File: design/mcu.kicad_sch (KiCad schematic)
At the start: 13 parts, among them U1 STM32F40X_LQFP64, X1 8m

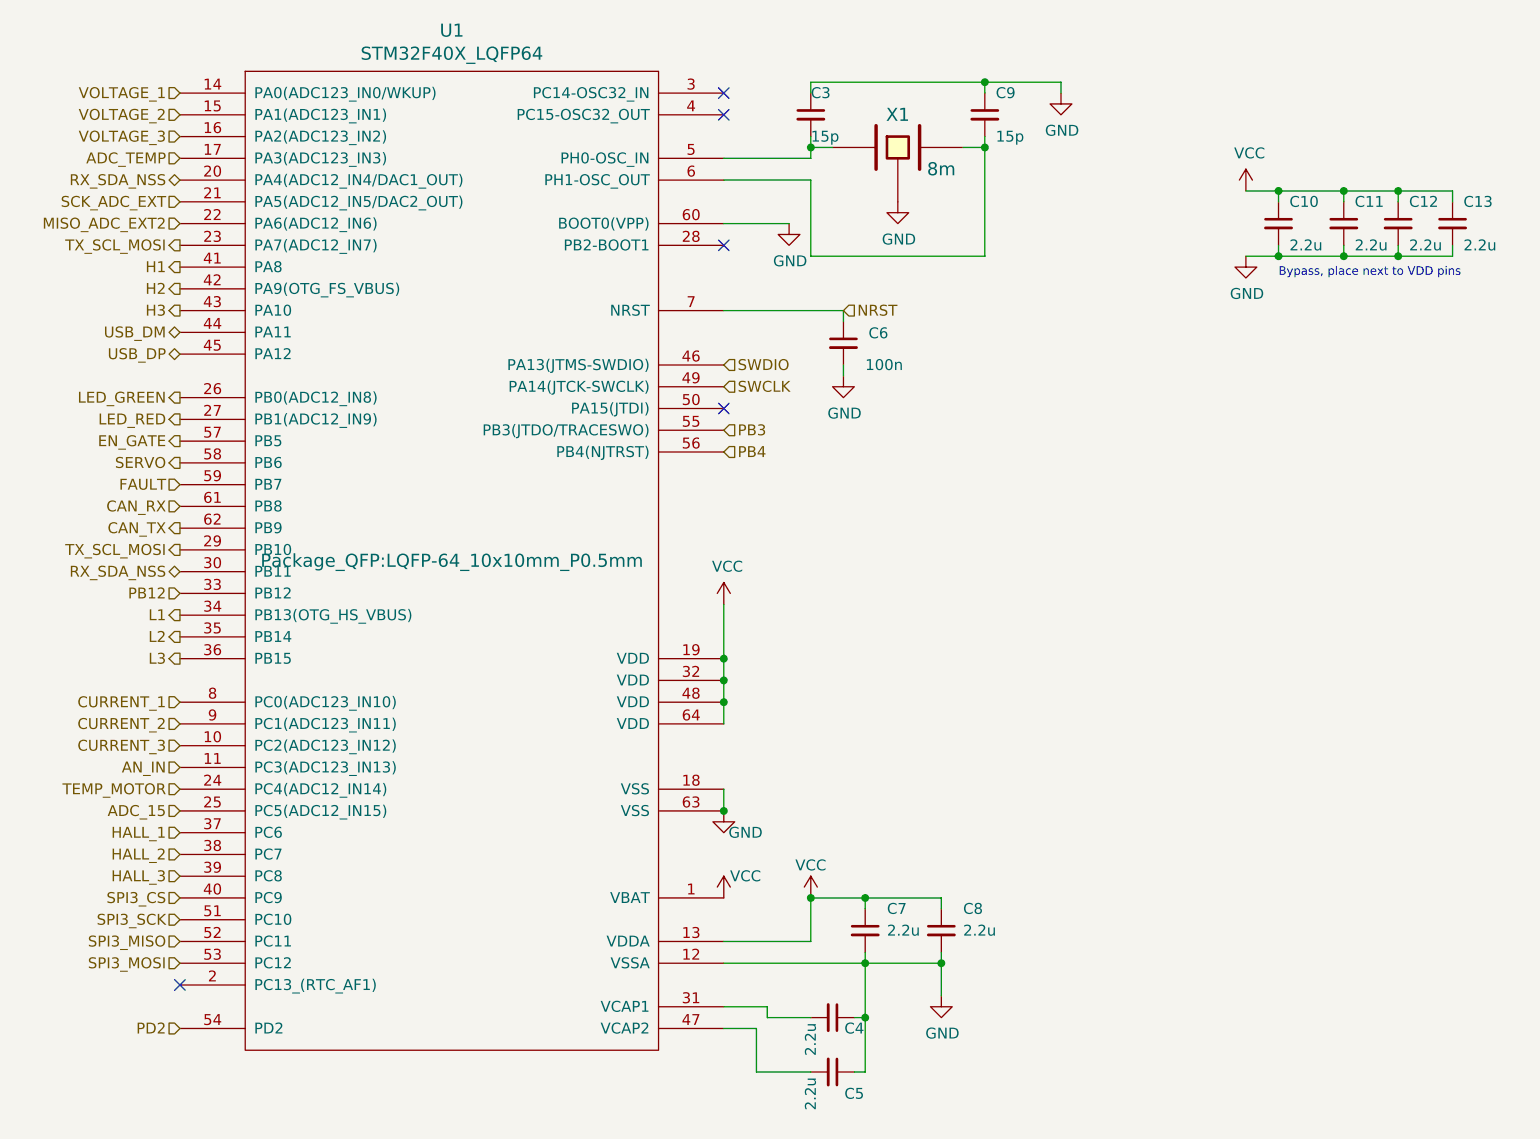
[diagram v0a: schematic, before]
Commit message: Impresión de esquemático en pdf
Impresión de la versión del esquemático en la carpeta /pdf
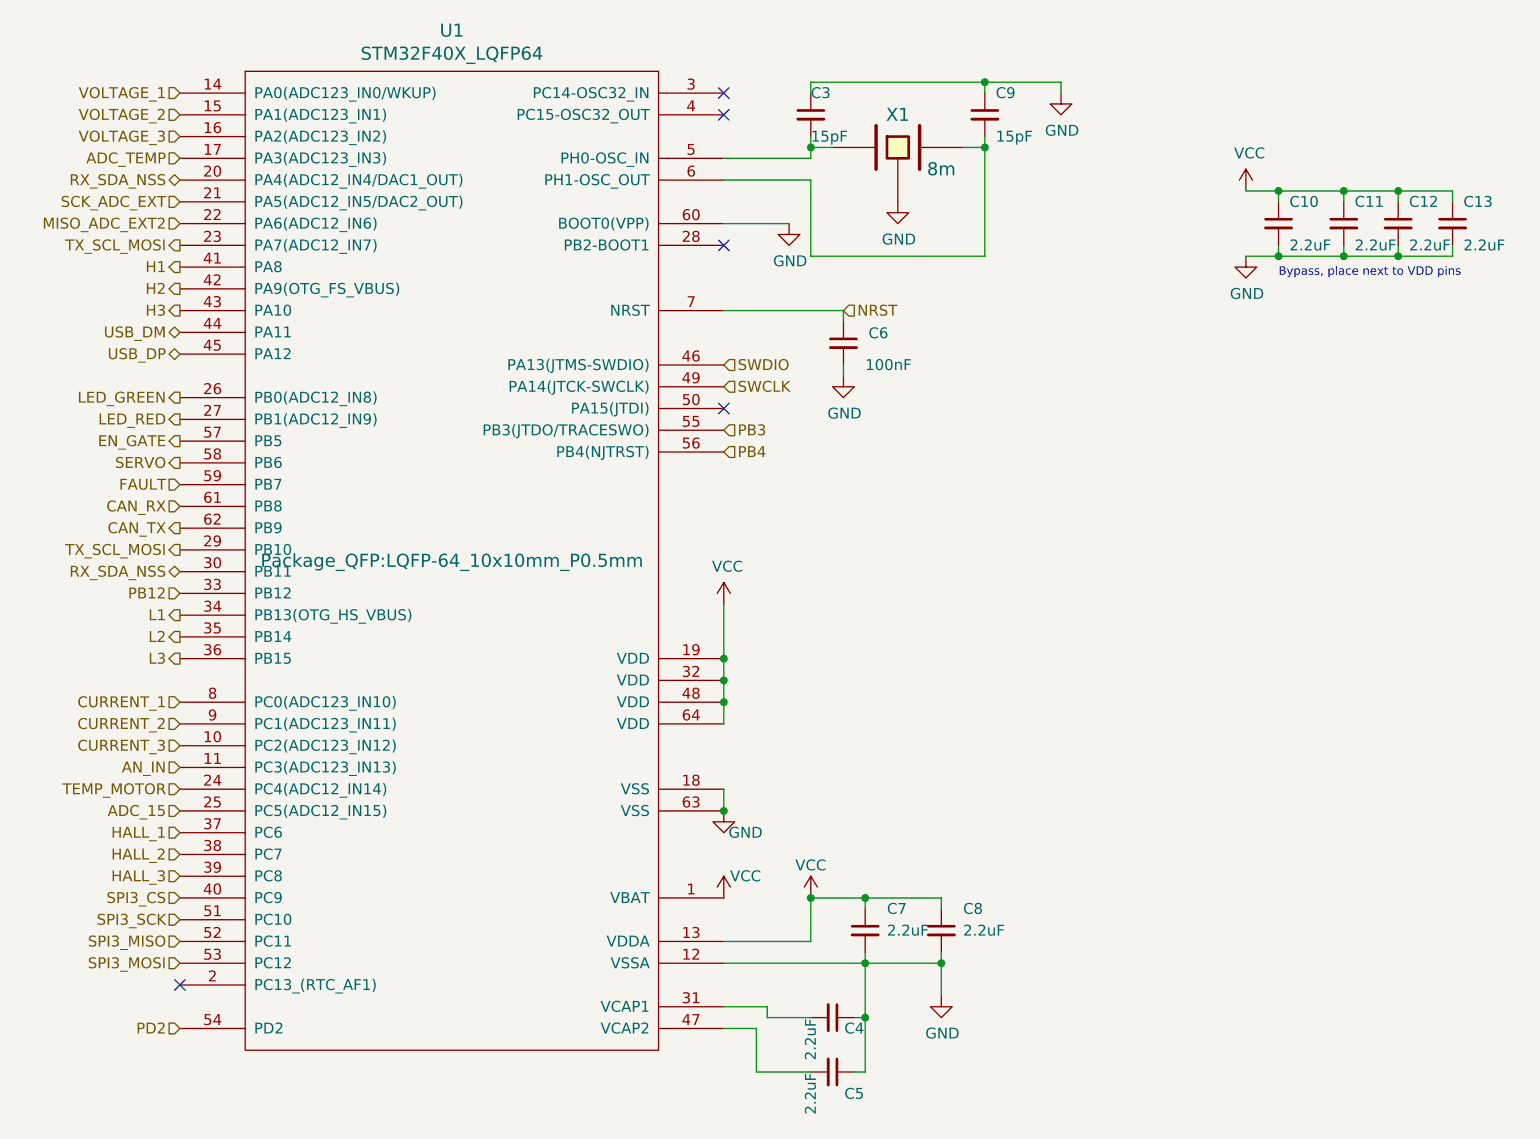
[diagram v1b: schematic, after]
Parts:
- C10, C11, C12, C13, C4, C5, C7, C8: value 2.2u -> 2.2uF
- C3, C9: value 15p -> 15pF
- C6: value 100n -> 100nF
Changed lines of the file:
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@@
 			)
 		)
-		(property "Value" "15p"
+		(property "Value" "15pF"
 			(at 195.58 36.83 0)
 			(effects
@@
 			)
 		)
-		(property "Value" "15p"
+		(property "Value" "15pF"
 			(at 217.17 36.83 0)
 			(effects
@@
 			)
 		)
-		(property "Value" "100n"
+		(property "Value" "100nF"
 			(at 201.93 63.5 0)
 			(effects
@@
 			)
 		)
-		(property "Value" "2.2u"
+		(property "Value" "2.2uF"
 			(at 204.47 129.54 0)
 			(effects
@@
 			)
 		)
-		(property "Value" "2.2u"
+		(property "Value" "2.2uF"
 			(at 213.36 129.54 0)
 			(effects
@@
 			)
 		)
-		(property "Value" "2.2u"
+		(property "Value" "2.2uF"
 			(at 195.58 142.24 0)
 			(effects
@@
 			)
 		)
-		(property "Value" "2.2u"
+		(property "Value" "2.2uF"
 			(at 195.58 148.59 0)
 			(effects
@@
 			)
 		)
-		(property "Value" "2.2u"
+		(property "Value" "2.2uF"
 			(at 251.46 49.53 0)
 			(effects
@@
 			)
 		)
-		(property "Value" "2.2u"
+		(property "Value" "2.2uF"
 			(at 259.08 49.53 0)
 			(effects
@@
 			)
 		)
-		(property "Value" "2.2u"
+		(property "Value" "2.2uF"
 			(at 265.43 49.53 0)
 			(effects
@@
 			)
 		)
-		(property "Value" "2.2u"
+		(property "Value" "2.2uF"
 			(at 271.78 49.53 0)
 			(effects

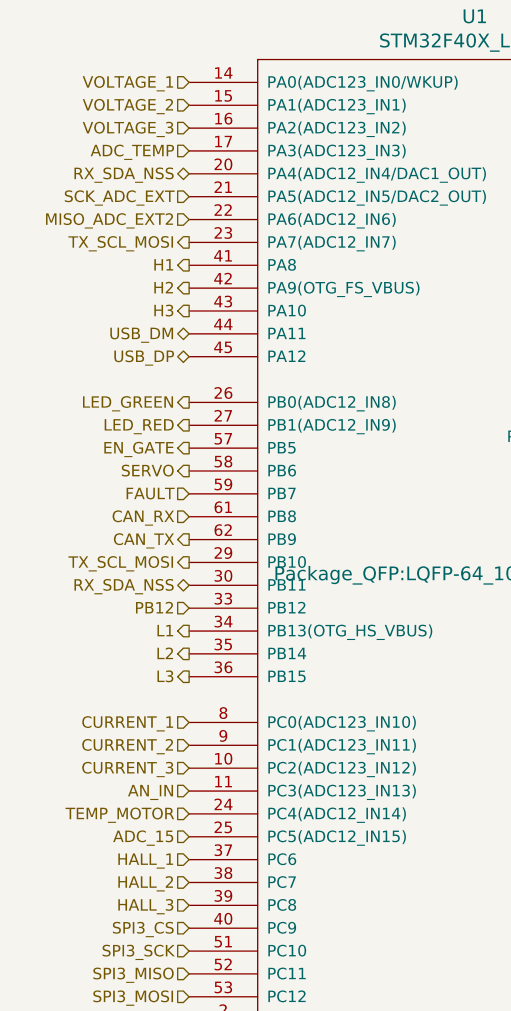
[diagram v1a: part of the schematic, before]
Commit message: Pequeños cambios
Se sacaron y se marcaron como NC:
	* CAN_TX y CAN_RX (no se usa CAN).
	* SERVO (no vamos a manejar servomotores).
	* ADC_15, MISO_ADC_EXT, TX_SCL_MOSI, RX_SDA_NSS, SCK_ADC_EXT (sin ADC externo ni acelerómetro).
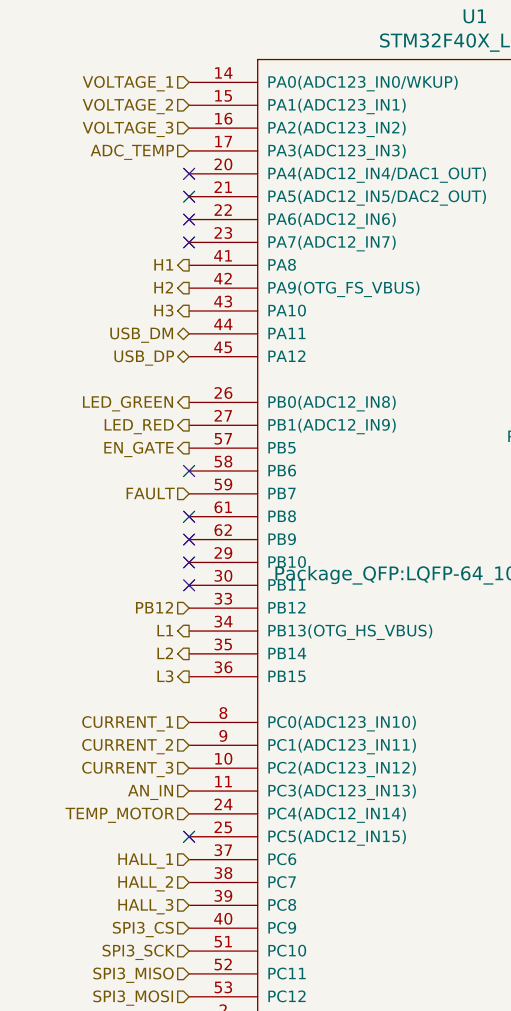
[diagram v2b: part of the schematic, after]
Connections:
- net ADC_15: no longer names the net of U1.25 (PC5(ADC12_IN15))
- net CAN_RX: no longer names the net of U1.61 (PB8)
- net CAN_TX: no longer names the net of U1.62 (PB9)
- net MISO_ADC_EXT2: no longer names the net of U1.22 (PA6(ADC12_IN6))
- net RX_SDA_NSS: no longer names the net of U1.20 (PA4(ADC12_IN4/DAC1_OUT))
- net RX_SDA_NSS: no longer U1.30 (PB11)
- net SCK_ADC_EXT: no longer names the net of U1.21 (PA5(ADC12_IN5/DAC2_OUT))
- net SERVO: no longer names the net of U1.58 (PB6)
- net TX_SCL_MOSI: no longer names the net of U1.23 (PA7(ADC12_IN7))
- net TX_SCL_MOSI: no longer U1.29 (PB10)
- no-connect marks 5 -> 15
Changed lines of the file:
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@@
+	)
+	(no_connect
+		(at 121.92 80.01)
+	)
+	(no_connect
+		(at 121.92 82.55)
+	)
+	(no_connect
+		(at 121.92 115.57)
+	)
+	(no_connect
+		(at 121.92 41.91)
 	)
 	(no_connect
@@
 	)
 	(no_connect
+		(at 121.92 85.09)
+	)
+	(no_connect
+		(at 121.92 44.45)
+	)
+	(no_connect
+		(at 121.92 49.53)
+	)
+	(no_connect
 		(at 185.42 68.58)
+	)
+	(no_connect
+		(at 121.92 87.63)
 	)
 	(no_connect
@@
 	)
 	(no_connect
+		(at 121.92 46.99)
+	)
+	(no_connect
 		(at 185.42 34.29)
+	)
+	(no_connect
+		(at 121.92 74.93)
 	)
 	(wire
@@
 		)
 	)
-	(hierarchical_label "RX_SDA_NSS"
-		(shape bidirectional)
-		(at 121.92 41.91 180)
-		(fields_autoplaced yes)
-		(effects
-			(font
-				(size 1.27 1.27)
-			)
-			(justify right)
-		)
-	)
 	(hierarchical_label "ADC_TEMP"
 		(shape input)
@@
 		)
 	)
-	(hierarchical_label "MISO_ADC_EXT2"
-		(shape input)
-		(at 121.92 46.99 180)
-		(fields_autoplaced yes)
-		(effects
-			(font
-				(size 1.27 1.27)
-			)
-			(justify right)
-		)
-	)
 	(hierarchical_label "AN_IN"
 		(shape input)
@@
 		)
 	)
-	(hierarchical_label "SERVO"
-		(shape output)
-		(at 121.92 74.93 180)
-		(fields_autoplaced yes)
-		(effects
-			(font
-				(size 1.27 1.27)
-			)
-			(justify right)
-		)
-	)
-	(hierarchical_label "SCK_ADC_EXT"
-		(shape input)
-		(at 121.92 44.45 180)
-		(fields_autoplaced yes)
-		(effects
-			(font
-				(size 1.27 1.27)
-			)
-			(justify right)
-		)
-	)
 	(hierarchical_label "PB4"
 		(shape input)
@@
 		)
 	)
-	(hierarchical_label "TX_SCL_MOSI"
-		(shape output)
-		(at 121.92 85.09 180)
-		(fields_autoplaced yes)
-		(effects
-			(font
-				(size 1.27 1.27)
-			)
-			(justify right)
-		)
-	)
 	(hierarchical_label "SWDIO"
 		(shape input)
@@
 		)
 	)
-	(hierarchical_label "TX_SCL_MOSI"
-		(shape output)
-		(at 121.92 49.53 180)
-		(fields_autoplaced yes)
-		(effects
-			(font
-				(size 1.27 1.27)
-			)
-			(justify right)
-		)
-	)
 	(hierarchical_label "SWCLK"
 		(shape input)
@@
 		)
 	)
-	(hierarchical_label "RX_SDA_NSS"
-		(shape bidirectional)
-		(at 121.92 87.63 180)
-		(fields_autoplaced yes)
-		(effects
-			(font
-				(size 1.27 1.27)
-			)
-			(justify right)
-		)
-	)
 	(hierarchical_label "TEMP_MOTOR"
 		(shape input)
@@
 		)
 	)
-	(hierarchical_label "CAN_TX"
-		(shape output)
-		(at 121.92 82.55 180)
-		(fields_autoplaced yes)
-		(effects
-			(font
-				(size 1.27 1.27)
-			)
-			(justify right)
-		)
-	)
 	(hierarchical_label "EN_GATE"
 		(shape output)
@@
 		)
 	)
-	(hierarchical_label "ADC_15"
-		(shape input)
-		(at 121.92 115.57 180)
-		(fields_autoplaced yes)
-		(effects
-			(font
-				(size 1.27 1.27)
-			)
-			(justify right)
-		)
-	)
 	(hierarchical_label "HALL_1"
 		(shape input)
@@
 		(fields_autoplaced yes)
 		(effects
-			(font
-				(size 1.27 1.27)
-			)
-			(justify right)
-		)
-	)
-	(hierarchical_label "CAN_RX"
-		(shape input)
-		(at 121.92 80.01 180)
-		(fields_autoplaced yes)
-		(effects

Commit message: Agrego MFR.Part # a capacitores
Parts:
- C10, C11, C12, C13, C4, C5, C7, C8: Manufacturer (none) -> Samsung Electro-Mechanics; Manufacturer Product Number  (none) -> CL10A225KO8NNNC
- C3, C9: Manufacturer (none) -> Samsung Electro-Mechanics; Manufacturer Product Number  (none) -> CL10C150JB8NNNC
- C6: Manufacturer (none) -> YAGEO; Manufacturer Product Number  (none) -> CC0603KRX7R9BB104
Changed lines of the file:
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@@
+			)
+		)
+		(property "Manufacturer" "Samsung Electro-Mechanics"
+			(at 195.58 34.29 0)
+			(effects
+				(font
+					(size 1.27 1.27)
+				)
+				(hide yes)
+			)
+		)
+		(property "Manufacturer Product Number " "CL10C150JB8NNNC"
+			(at 195.58 34.29 0)
+			(effects
+				(font
+					(size 1.27 1.27)
+				)
+				(hide yes)
 			)
 		)
@@
 			)
 		)
+		(property "Manufacturer" "Samsung Electro-Mechanics"
+			(at 215.9 34.29 0)
+			(effects
+				(font
+					(size 1.27 1.27)
+				)
+				(hide yes)
+			)
+		)
+		(property "Manufacturer Product Number " "CL10C150JB8NNNC"
+			(at 215.9 34.29 0)
+			(effects
+				(font
+					(size 1.27 1.27)
+				)
+				(hide yes)
+			)
+		)
 		(pin "1"
 		)
@@
 			)
 		)
+		(property "Manufacturer" "YAGEO"
+			(at 199.39 60.96 0)
+			(effects
+				(font
+					(size 1.27 1.27)
+				)
+				(hide yes)
+			)
+		)
+		(property "Manufacturer Product Number " "CC0603KRX7R9BB104"
+			(at 199.39 60.96 0)
+			(effects
+				(font
+					(size 1.27 1.27)
+				)
+				(hide yes)
+			)
+		)
 		(pin "2"
 		)
@@
 			)
 		)
+		(property "Manufacturer" "Samsung Electro-Mechanics"
+			(at 201.93 129.54 0)
+			(effects
+				(font
+					(size 1.27 1.27)
+				)
+				(hide yes)
+			)
+		)
+		(property "Manufacturer Product Number " "CL10A225KO8NNNC"
+			(at 201.93 129.54 0)
+			(effects
+				(font
+					(size 1.27 1.27)
+				)
+				(hide yes)
+			)
+		)
 		(pin "1"
 		)
@@
 			)
 		)
+		(property "Manufacturer" "Samsung Electro-Mechanics"
+			(at 210.82 129.54 0)
+			(effects
+				(font
+					(size 1.27 1.27)
+				)
+				(hide yes)
+			)
+		)
+		(property "Manufacturer Product Number " "CL10A225KO8NNNC"
+			(at 210.82 129.54 0)
+			(effects
+				(font
+					(size 1.27 1.27)
+				)
+				(hide yes)
+			)
+		)
 		(pin "1"
 		)
@@
 			)
 		)
+		(property "Manufacturer" "Samsung Electro-Mechanics"
+			(at 198.12 139.7 0)
+			(effects
+				(font
+					(size 1.27 1.27)
+				)
+				(hide yes)
+			)
+		)
+		(property "Manufacturer Product Number " "CL10A225KO8NNNC"
+			(at 198.12 139.7 0)
+			(effects
+				(font
+					(size 1.27 1.27)
+				)
+				(hide yes)
+			)
+		)
 		(pin "2"
 		)
@@
 			)
 		)
+		(property "Manufacturer" "Samsung Electro-Mechanics"
+			(at 198.12 146.05 0)
+			(effects
+				(font
+					(size 1.27 1.27)
+				)
+				(hide yes)
+			)
+		)
+		(property "Manufacturer Product Number " "CL10A225KO8NNNC"
+			(at 198.12 146.05 0)
+			(effects
+				(font
+					(size 1.27 1.27)
+				)
+				(hide yes)
+			)
+		)
 		(pin "1"
 		)
@@
 			)
 		)
+		(property "Manufacturer" "Samsung Electro-Mechanics"
+			(at 250.19 46.99 0)
+			(effects
+				(font
+					(size 1.27 1.27)
+				)
+				(hide yes)
+			)
+		)
+		(property "Manufacturer Product Number " "CL10A225KO8NNNC"
+			(at 250.19 46.99 0)
+			(effects
+				(font
+					(size 1.27 1.27)
+				)
+				(hide yes)
+			)
+		)
 		(pin "2"
 		)
@@
 			)
 		)
+		(property "Manufacturer" "Samsung Electro-Mechanics"
+			(at 257.81 46.99 0)
+			(effects
+				(font
+					(size 1.27 1.27)
+				)
+				(hide yes)
+			)
+		)
+		(property "Manufacturer Product Number " "CL10A225KO8NNNC"
+			(at 257.81 46.99 0)
+			(effects
+				(font
+					(size 1.27 1.27)
+				)
+				(hide yes)
+			)
+		)
 		(pin "1"
 		)
@@
 			)
 		)
+		(property "Manufacturer" "Samsung Electro-Mechanics"
+			(at 264.16 46.99 0)
+			(effects
+				(font
+					(size 1.27 1.27)
+				)
+				(hide yes)
+			)
+		)
+		(property "Manufacturer Product Number " "CL10A225KO8NNNC"
+			(at 264.16 46.99 0)
+			(effects
+				(font
+					(size 1.27 1.27)
+				)
+				(hide yes)
+			)
+		)
 		(pin "1"
 		)
@@
 			(at 270.51 46.99 0)
 			(effects
+				(font
+					(size 1.27 1.27)
+				)
+				(hide yes)
+			)
+		)
+		(property "Manufacturer" "Samsung Electro-Mechanics"
+			(at 270.51 46.99 0)
+			(effects
+				(font
+					(size 1.27 1.27)
+				)
+				(hide yes)
+			)
+		)
+		(property "Manufacturer Product Number " "CL10A225KO8NNNC"
+			(at 270.51 46.99 0)
+			(effects

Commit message: Agregue Manufacturer Product Numbers
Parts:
- U1: Manufacturer (none) -> STMicroelectronics; Manufacturer Product Number  (none) -> STM32F401RCT6TR
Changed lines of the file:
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@@
+			)
+		)
+		(property "Manufacturer" " STMicroelectronics"
+			(at 153.67 86.36 0)
+			(effects
+				(font
+					(size 1.27 1.27)
+				)
+				(hide yes)
+			)
+		)
+		(property "Manufacturer Product Number " "STM32F401RCT6TR"
+			(at 153.67 86.36 0)
+			(effects
+				(font
+					(size 1.27 1.27)
+				)
+				(hide yes)
 			)
 		)

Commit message: Agregue Manufacturer Product Number
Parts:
- removed X1: 8m, symbol ESCX-cache:crf_1{colon}CRYSTAL_GROUND_PIN
- added X1: 8MHz, Crystal:Crystal_SMD_HC49-SD, symbol Device:Crystal_Small
- renumbered C11 to C10, C12 to C11, C13 to C12, C3 to C2, C4 to C3, C5 to C4, C6 to C5, C7 to C6, C8 to C7, C9 to C8, C10 to C9
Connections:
- net at C2.2, U1.5 (PH0-OSC_IN): now also X1.2
- net at C8.2, U1.6 (PH1-OSC_OUT): now also X1.1
